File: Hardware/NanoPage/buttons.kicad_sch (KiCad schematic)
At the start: 12 parts

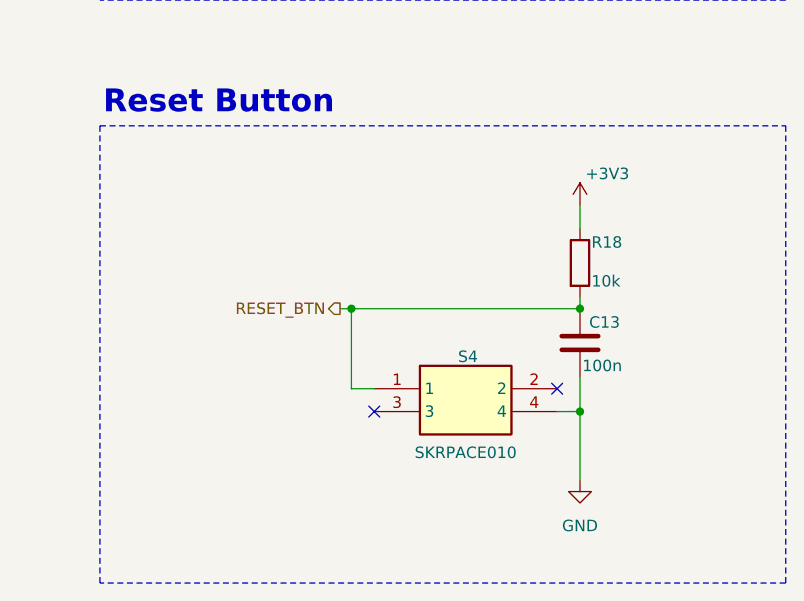
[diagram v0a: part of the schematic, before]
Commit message: fix: Fix wrong footprint
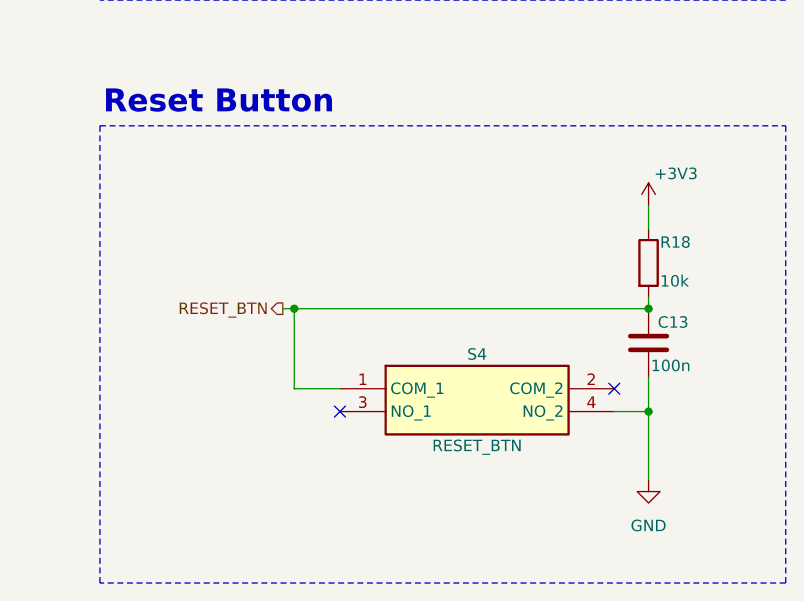
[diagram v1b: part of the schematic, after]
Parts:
- removed S4: SKRPACE010, SKRPARE010:SKRPARE010, symbol SKRPARE010:SKRPARE010
- added S4: RESET_BTN, PTS526SM15SMTR2LFS, symbol PTS526SM15SMTR2:PTS526SM15SMTR2_LFS
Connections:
- net GND: now also S4.4 (NO_2)
- net RESET_BTN: now also S4.1 (COM_1)
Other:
- moved on the sheet: C13, R18

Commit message: feat: Add an external button connector and fix some issues
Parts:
- added J6: ext_buttons_conn, Personal Library:HC-FPC-05-09-5RLTAG, symbol Connector_Generic:Conn_01x07
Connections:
- net +3V3: now also J6.4 (Pin_4)
- net ACTION_BTN: now also J6.2 (Pin_2)
- net GND: now also J6.5 (Pin_5)
- net NEXT_BTN: now also J6.1 (Pin_1)
- net PREV_BTN: now also J6.3 (Pin_3)
- no-connect marks 2 -> 4
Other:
- note added: "External Buttons connector"
- moved on the sheet: C10, C11, C12, C13, R15, R16, R17, R18, S1, S2, S3, S4

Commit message: feat: vendor custom KiCad symbols, footprints and 3D models into the project
Move all downloaded and self-made parts into a project-local NanoPage
library (libraries/NanoPage.{kicad_sym,pretty,3dshapes}) referenced via
${KIPRJMOD}, so the design opens on any machine without the global
external_libraries folder. KiCad built-in parts are unchanged.
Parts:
- J6: footprint Personal Library:HC-FPC-05-09-5RLTAG -> NanoPage:HC-FPC-05-09-5RLTAG
- S1, S2, S3: footprint SKRTLAE010:SKRTLAE010 -> NanoPage:SKRTLAE010; symbol SKRTLAE010:SKRTLAE010 -> NanoPage:SKRTLAE010
- S4: footprint PTS526SM15SMTR2LFS -> NanoPage:PTS526SM15SMTR2LFS; symbol PTS526SM15SMTR2:PTS526SM15SMTR2_LFS -> NanoPage:PTS526SM15SMTR2_LFS
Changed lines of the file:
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@@
 	)
 	(symbol
-		(lib_id "SKRTLAE010:SKRTLAE010")
+		(lib_id "NanoPage:SKRTLAE010")
 		(at 127 67.31 0)
 		(unit 1)
@@
 			)
 		)
-		(property "Footprint" "SKRTLAE010:SKRTLAE010"
+		(property "Footprint" "NanoPage:SKRTLAE010"
 			(at 146.05 162.23 0)
 			(hide yes)
@@
 	(symbol
 		(lib_name "SKRTLAE010_1")
-		(lib_id "SKRTLAE010:SKRTLAE010")
+		(lib_id "NanoPage:SKRTLAE010")
 		(at 35.56 132.08 0)
 		(unit 1)
@@
 			)
 		)
-		(property "Footprint" "SKRTLAE010:SKRTLAE010"
+		(property "Footprint" "NanoPage:SKRTLAE010"
 			(at 54.61 227 0)
 			(hide yes)
@@
 	)
 	(symbol
-		(lib_id "SKRTLAE010:SKRTLAE010")
+		(lib_id "NanoPage:SKRTLAE010")
 		(at 35.56 67.31 0)
 		(unit 1)
@@
 			)
 		)
-		(property "Footprint" "SKRTLAE010:SKRTLAE010"
+		(property "Footprint" "NanoPage:SKRTLAE010"
 			(at 54.61 162.23 0)
 			(hide yes)
@@
 	)
 	(symbol
-		(lib_id "PTS526SM15SMTR2:PTS526SM15SMTR2_LFS")
+		(lib_id "NanoPage:PTS526SM15SMTR2_LFS")
 		(at 137.16 135.89 0)
 		(unit 1)
@@
 			)
 		)
-		(property "Footprint" "PTS526SM15SMTR2LFS"
+		(property "Footprint" "NanoPage:PTS526SM15SMTR2LFS"
 			(at 163.83 230.81 0)
 			(hide yes)
@@
 			)
 		)
-		(property "Footprint" "Personal Library:HC-FPC-05-09-5RLTAG"
+		(property "Footprint" "NanoPage:HC-FPC-05-09-5RLTAG"
 			(at 246.38 71.12 0)
 			(hide yes)
